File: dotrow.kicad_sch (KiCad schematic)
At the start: 48 parts, among them J1 Conn_01x02_Pin, J2 Conn_01x02_Pin, J3 Conn_01x02_Pin, J4 Conn_01x12_Pin, U5 74HC595

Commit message: valid 13 row layout
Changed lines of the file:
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@@
 	(paper "A4")
 	(junction
+		(at 179.07 86.36)
+		(diameter 0)
+		(color 0 0 0 0)
+	)
+	(junction
 		(at 191.77 73.66)
 		(diameter 0)
@@
 	)
 	(junction
+		(at 179.07 88.9)
+		(diameter 0)
+		(color 0 0 0 0)
+	)
+	(junction
 		(at 50.8 29.21)
 		(diameter 0)
@@
 	(junction
 		(at 69.85 26.67)
+		(diameter 0)
+		(color 0 0 0 0)
+	)
+	(junction
+		(at 179.07 78.74)
 		(diameter 0)
 		(color 0 0 0 0)
@@
 	(wire
 		(pts
+			(xy 179.07 86.36) (xy 212.09 86.36)
+		)
+		(stroke
+			(width 0)
+			(type default)
+		)
+	)
+	(wire
+		(pts
 			(xy 74.93 41.91) (xy 69.85 41.91)
 		)
@@
 	(wire
 		(pts
-			(xy 154.94 88.9) (xy 214.63 88.9)
+			(xy 154.94 88.9) (xy 179.07 88.9)
 		)
 		(stroke
@@
 	(wire
 		(pts
+			(xy 179.07 91.44) (xy 179.07 88.9)
+		)
+		(stroke
+			(width 0)
+			(type default)
+		)
+	)
+	(wire
+		(pts
 			(xy 234.95 73.66) (xy 240.03 73.66)
 		)
@@
 	(wire
 		(pts
+			(xy 179.07 78.74) (xy 200.66 78.74)
+		)
+		(stroke
+			(width 0)
+			(type default)
+		)
+	)
+	(wire
+		(pts
 			(xy 92.71 149.86) (xy 106.68 149.86)
 		)
@@
 	(wire
 		(pts
-			(xy 167.64 86.36) (xy 212.09 86.36)
+			(xy 167.64 86.36) (xy 179.07 86.36)
 		)
 		(stroke
@@
 	(wire
 		(pts
+			(xy 179.07 83.82) (xy 179.07 86.36)
+		)
+		(stroke
+			(width 0)
+			(type default)
+		)
+	)
+	(wire
+		(pts
 			(xy 40.64 129.54) (xy 40.64 133.35)
 		)
@@
 	(wire
 		(pts
+			(xy 179.07 88.9) (xy 214.63 88.9)
+		)
+		(stroke
+			(width 0)
+			(type default)
+		)
+	)
+	(wire
+		(pts
 			(xy 45.72 29.21) (xy 50.8 29.21)
 		)
@@
 	(wire
 		(pts
+			(xy 182.88 83.82) (xy 179.07 83.82)
+		)
+		(stroke
+			(width 0)
+			(type default)
+		)
+	)
+	(wire
+		(pts
 			(xy 144.78 64.77) (xy 144.78 68.58)
 		)
@@
 	(wire
 		(pts
+			(xy 182.88 81.28) (xy 179.07 81.28)
+		)
+		(stroke
+			(width 0)
+			(type default)
+		)
+	)
+	(wire
+		(pts
 			(xy 50.8 114.3) (xy 74.93 114.3)
 		)
@@
 	(wire
 		(pts
+			(xy 184.15 91.44) (xy 179.07 91.44)
+		)
+		(stroke
+			(width 0)
+			(type default)
+		)
+	)
+	(wire
+		(pts
 			(xy 69.85 41.91) (xy 69.85 39.37)
 		)
@@
 	(wire
 		(pts
+			(xy 179.07 81.28) (xy 179.07 78.74)
+		)
+		(stroke
+			(width 0)
+			(type default)
+		)
+	)
+	(wire
+		(pts
 			(xy 232.41 113.03) (xy 232.41 107.95)
 		)
@@
 	(wire
 		(pts
-			(xy 154.94 78.74) (xy 200.66 78.74)
+			(xy 154.94 78.74) (xy 179.07 78.74)
 		)
 		(stroke
@@
 		)
 	)
+	(global_label "LATCH"
+		(shape input)
+		(at 182.88 83.82 0)
+		(fields_autoplaced yes)
+		(effects
+			(font
+				(size 1.27 1.27)
+			)
+			(justify left)
+		)
+		(property "Intersheetrefs" "${INTERSHEET_REFS}"
+			(at 191.55 83.82 0)
+			(effects
+				(font
+					(size 1.27 1.27)
+				)
+				(justify left)
+				(hide yes)
+			)
+		)
+	)
+	(global_label "CLK"
+		(shape input)
+		(at 182.88 81.28 0)
+		(fields_autoplaced yes)
+		(effects
+			(font
+				(size 1.27 1.27)
+			)
+			(justify left)
+		)
+		(property "Intersheetrefs" "${INTERSHEET_REFS}"
+			(at 189.4333 81.28 0)
+			(effects
+				(font
+					(size 1.27 1.27)
+				)
+				(justify left)
+				(hide yes)
+			)
+		)
+	)
+	(global_label "OE*"
+		(shape input)
+		(at 184.15 91.44 0)
+		(fields_autoplaced yes)
+		(effects
+			(font
+				(size 1.27 1.27)
+			)
+			(justify left)
+		)
+		(property "Intersheetrefs" "${INTERSHEET_REFS}"
+			(at 190.5823 91.44 0)
+			(effects
+				(font
+					(size 1.27 1.27)
+				)
+				(justify left)
+				(hide yes)
+			)
+		)
+	)

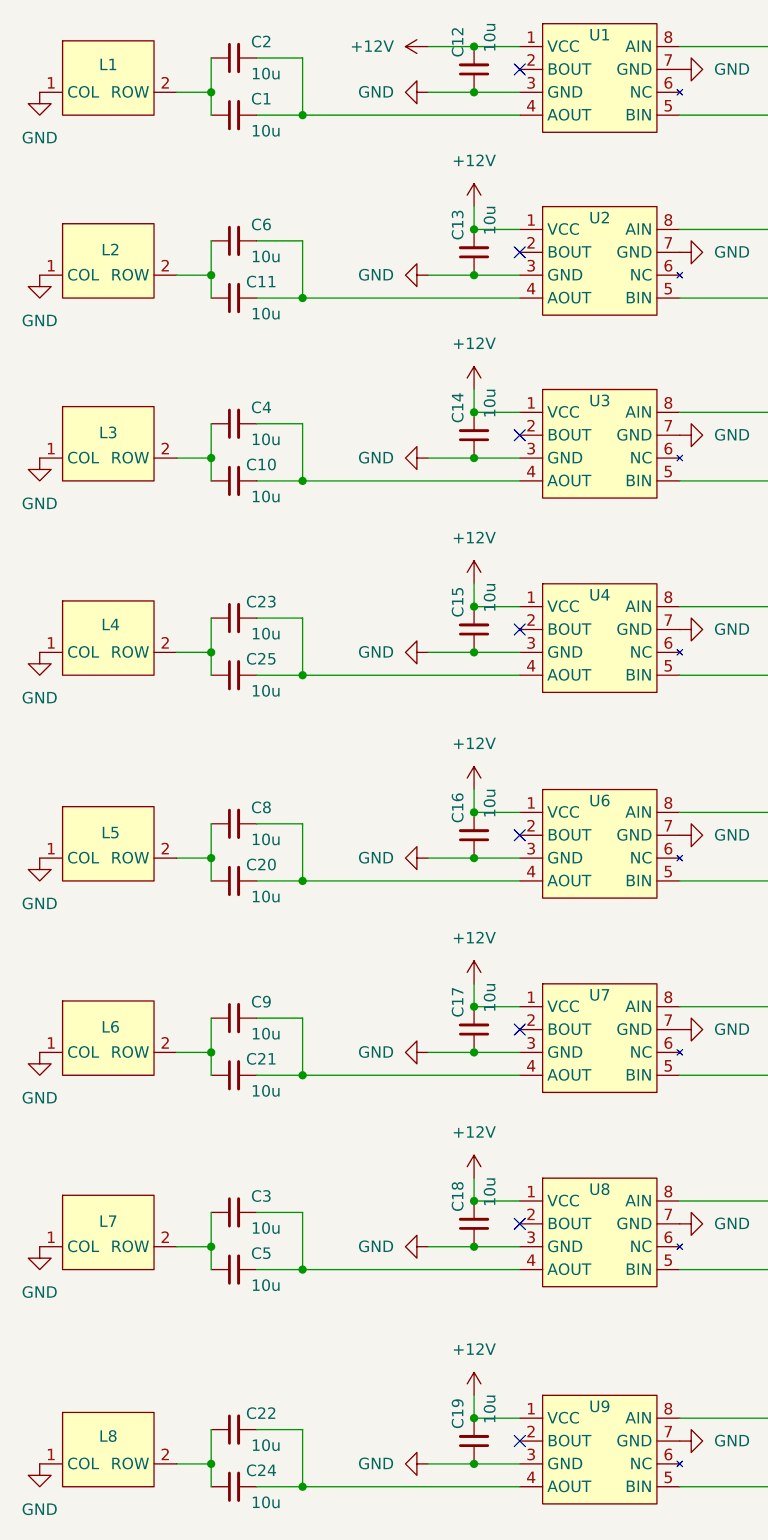
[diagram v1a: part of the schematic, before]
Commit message: Start on switching to electrolytics
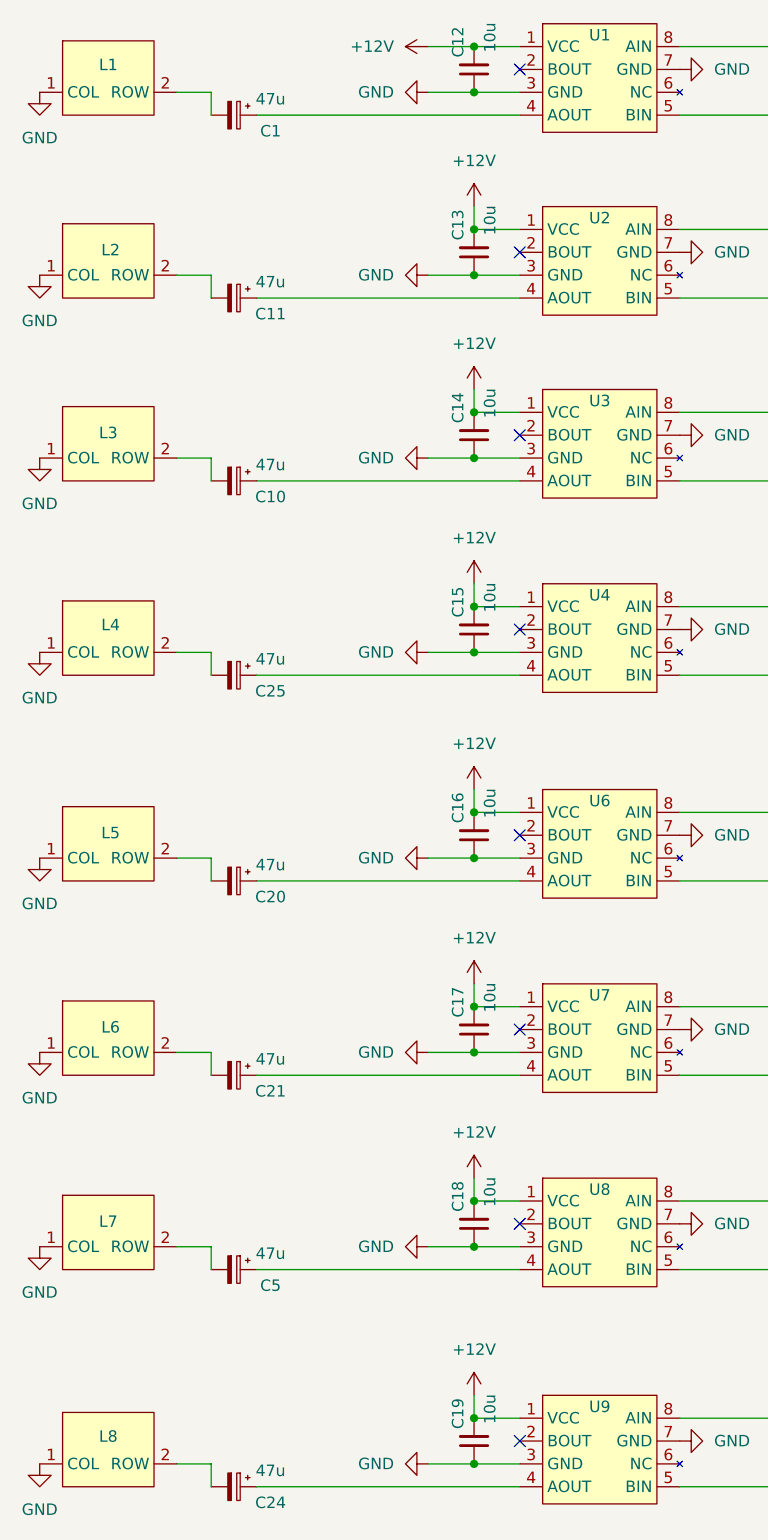
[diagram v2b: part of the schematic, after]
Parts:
- removed C2, C22, C23, C3, C4, C6, C8, C9: 10u, Capacitor_SMD:C_0805_2012Metric, symbol Device:C_Small
- C1, C10, C11, C20, C21, C24, C25, C5: value 10u -> 47u; footprint Capacitor_SMD:C_0805_2012Metric -> Flipdot:CP_Elec_5x5.4_slim; symbol Device:C_Small -> Device:C_Polarized_Small
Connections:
- net at U1.4 (AOUT): now also C1.1; no longer C1.2
- net at C5.1: now also U8.4 (AOUT); no longer L7.2 (ROW)
- net at C5.2: now also L7.2 (ROW); no longer U8.4 (AOUT)
- net at C24.1: now also U9.4 (AOUT); no longer L8.2 (ROW)
- net at C24.2: now also L8.2 (ROW); no longer U9.4 (AOUT)
- net at C11.1: now also U2.4 (AOUT); no longer L2.2 (ROW)
- net at C11.2: now also L2.2 (ROW); no longer U2.4 (AOUT)
- net at C25.1: now also U4.4 (AOUT); no longer L4.2 (ROW)
- net at C25.2: now also L4.2 (ROW); no longer U4.4 (AOUT)
- net at L1.2 (ROW): now also C1.2; no longer C1.1
- net at C10.1: now also U3.4 (AOUT); no longer L3.2 (ROW)
- net at C10.2: now also L3.2 (ROW); no longer U3.4 (AOUT)
- net at U6.4 (AOUT): now also C20.1; no longer C20.2
- net at C21.1: now also U7.4 (AOUT); no longer L6.2 (ROW)
- net at C21.2: now also L6.2 (ROW); no longer U7.4 (AOUT)
- net at L5.2 (ROW): now also C20.2; no longer C20.1

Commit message: add mosfet
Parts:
- L1, L2, L3, L4, L5, L6, L7, L8, U1, U2, U3, U4, U6, U7, U8, U9: value ~ -> (none)

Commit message: replace data connectors with just two 5-pin ZH
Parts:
- removed J4: Conn_01x12_Pin, Connector_JST:JST_ZH_B6B-ZR_1x06_P1.50mm_Vertical, symbol Connector:Conn_01x12_Pin
